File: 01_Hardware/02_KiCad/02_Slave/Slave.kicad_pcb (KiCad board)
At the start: 2 copper layers, 12 parts, among them J1 Screw_Terminal_01x04, J2 Conn_01x30_Female, J3 Screw_Terminal_01x04, J4 Conn_01x30_Female, Q1 AO3400A, Q2 AO3400A, U1 LM393

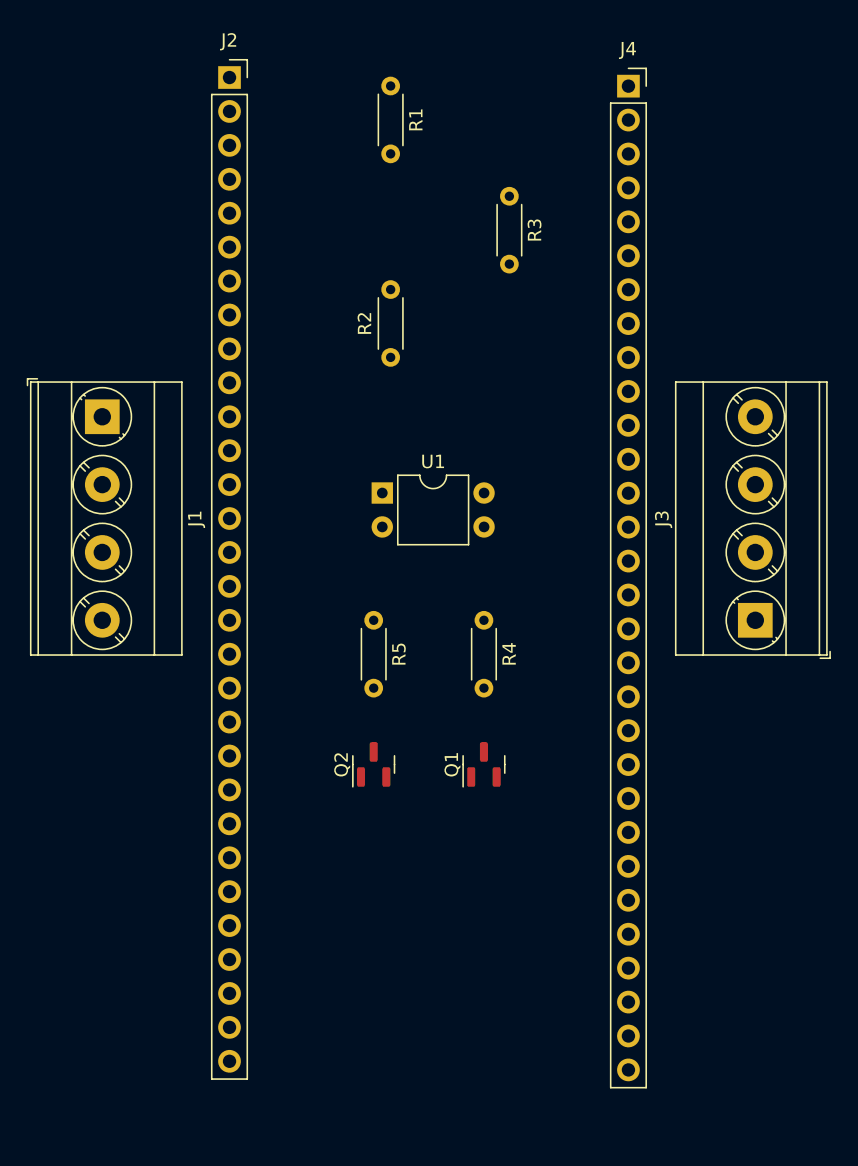
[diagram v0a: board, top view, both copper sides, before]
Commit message: KiCad Slave Update, now routed
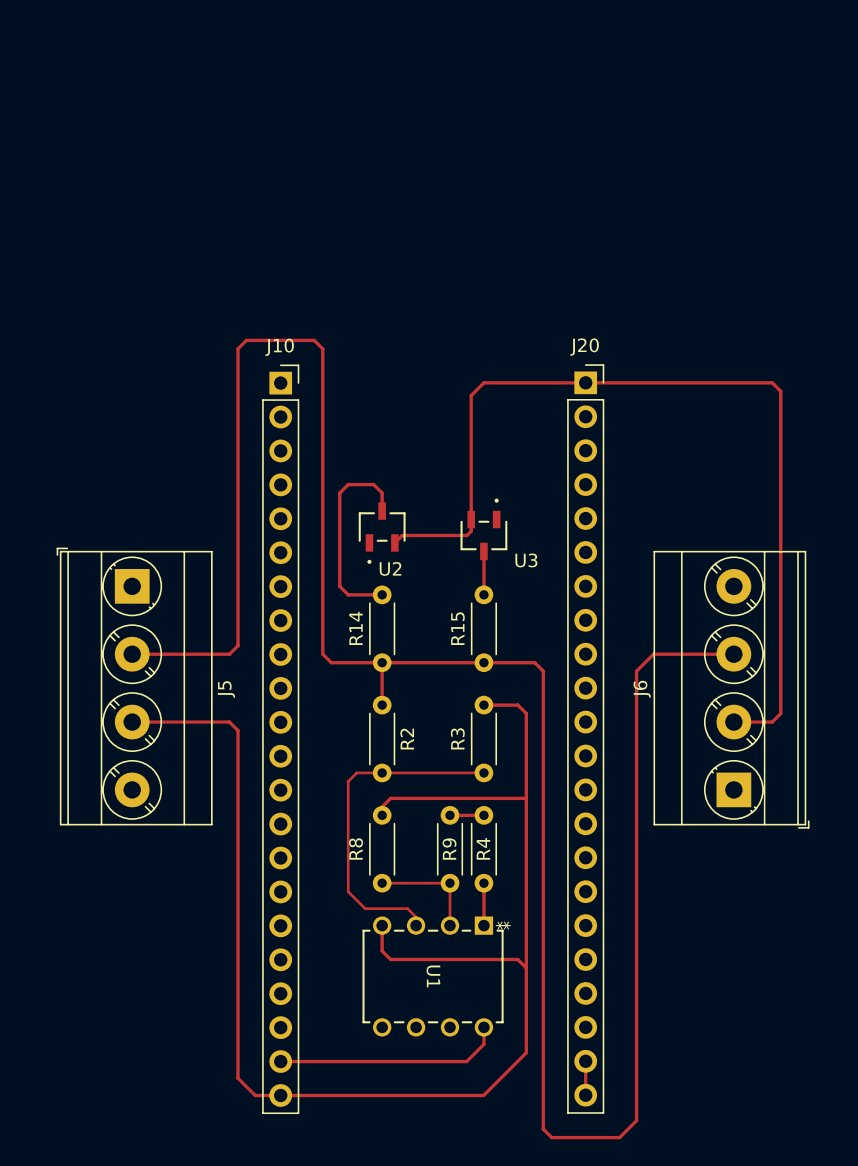
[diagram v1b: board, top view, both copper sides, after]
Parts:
- removed J1, J3: Screw_Terminal_01x04, TerminalBlock_Phoenix:TerminalBlock_Phoenix_MKDS-3-4-5.08_1x04_P5.08mm_Horizontal
- removed J2, J4: Conn_01x30_Female, Connector_PinSocket_2.54mm:PinSocket_1x30_P2.54mm_Vertical
- removed Q1, Q2: AO3400A, Package_TO_SOT_SMD:SOT-23
- removed R1: 1k, Resistor_THT:R_Axial_DIN0204_L3.6mm_D1.6mm_P5.08mm_Horizontal
- removed R5: 400, Resistor_THT:R_Axial_DIN0204_L3.6mm_D1.6mm_P5.08mm_Horizontal
- added J10: Conn_01x22_Female, Connector_PinSocket_2.54mm:PinSocket_1x22_P2.54mm_Vertical, F.Cu at (161.9, 88.3)
- added J20: Conn_01x22_Female, Connector_PinSocket_2.54mm:PinSocket_1x22_P2.54mm_Vertical, F.Cu at (184.8, 88.3)
- added J5: Screw_Terminal_01x04, TerminalBlock_Phoenix:TerminalBlock_Phoenix_MKDS-3-4-5.08_1x04_P5.08mm_Horizontal, F.Cu at (150.8, 103.5)
- added J6: Screw_Terminal_01x04, TerminalBlock_Phoenix:TerminalBlock_Phoenix_MKDS-3-4-5.08_1x04_P5.08mm_Horizontal, F.Cu at (195.9, 118.7)
- added R14: 400, Resistor_THT:R_Axial_DIN0204_L3.6mm_D1.6mm_P5.08mm_Horizontal, F.Cu at (169.5, 109.2)
- added R15: 400, Resistor_THT:R_Axial_DIN0204_L3.6mm_D1.6mm_P5.08mm_Horizontal, F.Cu at (177.2, 109.2)
- added R8: 14.3k, Resistor_THT:R_Axial_DIN0204_L3.6mm_D1.6mm_P5.08mm_Horizontal, F.Cu at (169.5, 125.7)
- added R9: 10k, Resistor_THT:R_Axial_DIN0204_L3.6mm_D1.6mm_P5.08mm_Horizontal, F.Cu at (174.6, 120.7)
- added U2: AO3400A, AO3400A:SOT-23-3L_AOS, F.Cu at (169.5, 99.1)
- added U3: AO3400A, AO3400A:SOT-23-3L_AOS, F.Cu at (177.2, 99.7)
- R2: value 4k -> 10k
- R4: value 400 -> 10k
- U1: value LM393 -> LM393P; footprint Package_DIP:DIP-4_W7.62mm -> LM393:P8
- moved R3 43.2 mm to (177.2, 117.5), turned to 90 degrees
- moved U1 33.3 mm to (177.2, 128.9), turned to -90 degrees
- moved R2 26.0 mm to (169.5, 112.4), turned to -90 degrees
- moved R4 19.7 mm to (177.2, 125.7), turned to 90 degrees
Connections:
- R2 pad 1: Net-(R1-Pad2) -> Bus
- R2 pad 2: GND -> LM393_IN+
- R3 pad 1: Net-(R3-Pad1) -> LM393_IN+
- R3 pad 2: Net-(R3-Pad2) -> GND
- R4 pad 1: Bus -> LM393_Out
- R4 pad 2: Net-(R4-Pad2) -> 3.3V
- U1 pad 1: Net-(R3-Pad2) -> LM393_Out
- U1 pad 2: Net-(R1-Pad2) -> LM393_IN-
- U1 pad 3: Bus -> LM393_IN+
- U1 pad 4: (no net) -> GND
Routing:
- net GND: track 0.00 -> 181.9 mm
- net Bus: track 0.00 -> 163.9 mm
- net LM393_IN+: track 0.00 -> 25.2 mm
- net 5V: track 0.00 -> 17.0 mm
- net Net-(R14-Pad2): track 0.00 -> 15.5 mm
- net LM393_IN-: track 0.00 -> 8.26 mm
- net Net-(R15-Pad2): track 0.00 -> 3.25 mm
- net LM393_Out: track 0.00 -> 3.17 mm
- net 3.3V: track 0.00 -> 2.54 mm
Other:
- board text removed: "Slave"
